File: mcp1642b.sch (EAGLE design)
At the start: 6 parts, among them U11 MCP1642B

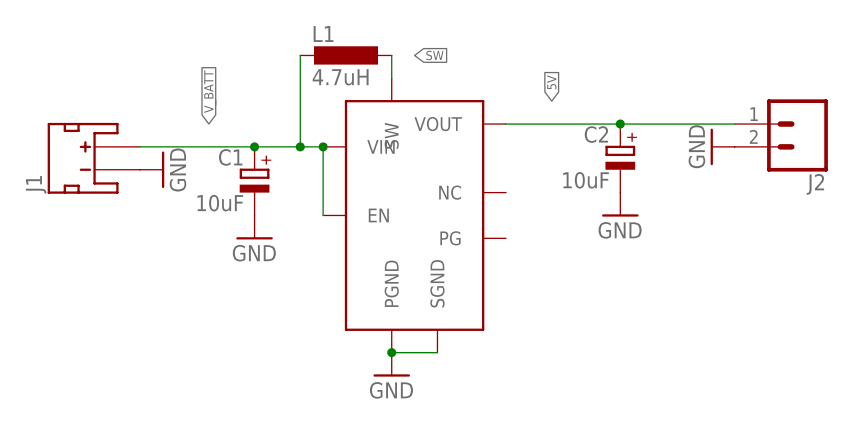
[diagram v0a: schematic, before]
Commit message: Wed  6 Mar 2019 10:52:50 EST - added AAA alkaline version of TPS61032
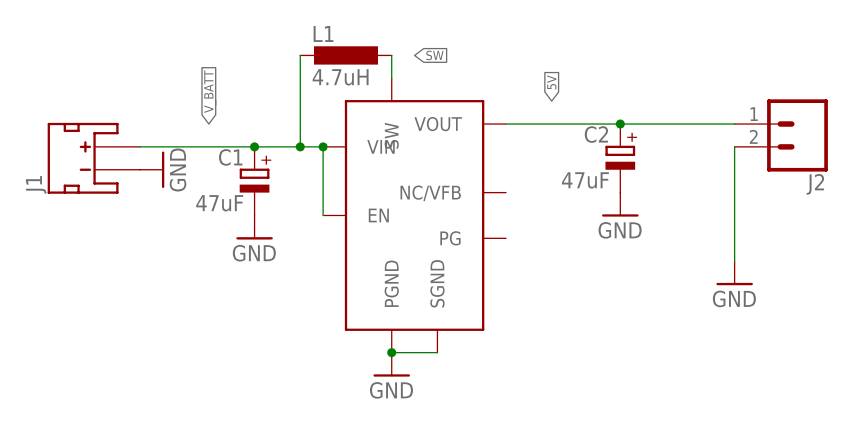
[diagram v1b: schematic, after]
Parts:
- C1, C2: value 10uF -> 47uF
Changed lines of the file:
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@@
 <?xml version="1.0" encoding="utf-8"?>
 <!DOCTYPE eagle SYSTEM "eagle.dtd">
-<eagle version="9.0.1">
+<eagle version="9.0.0">
 <drawing>
 <settings>
@@
 <grid distance="0.1" unitdist="inch" unit="inch" style="lines" multiple="1" display="no" altdistance="0.01" altunitdist="inch" altunit="inch"/>
 <layers>
-<layer number="1" name="Top" color="4" fill="1" visible="yes" active="no"/>
-<layer number="2" name="Route2" color="1" fill="3" visible="yes" active="no"/>
-<layer number="15" name="Route15" color="4" fill="6" visible="yes" active="no"/>
-<layer number="16" name="Bottom" color="1" fill="1" visible="yes" active="no"/>
-<layer number="17" name="Pads" color="2" fill="1" visible="yes" active="no"/>
-<layer number="18" name="Vias" color="2" fill="1" visible="yes" active="no"/>
-<layer number="19" name="Unrouted" color="6" fill="1" visible="yes" active="no"/>
-<layer number="20" name="Dimension" color="24" fill="1" visible="yes" active="no"/>
-<layer number="21" name="tPlace" color="7" fill="1" visible="yes" active="no"/>
-<layer number="22" name="bPlace" color="7" fill="1" visible="yes" active="no"/>
-<layer number="23" name="tOrigins" color="15" fill="1" visible="yes" active="no"/>
-<layer number="24" name="bOrigins" color="15" fill="1" visible="yes" active="no"/>
-<layer number="25" name="tNames" color="7" fill="1" visible="yes" active="no"/>
-<layer number="26" name="bNames" color="7" fill="1" visible="yes" active="no"/>
-<layer number="27" name="tValues" color="7" fill="1" visible="yes" active="no"/>
-<layer number="28" name="bValues" color="7" fill="1" visible="yes" active="no"/>
+<layer number="1" name="Top" color="4" fill="1" visible="no" active="no"/>
+<layer number="2" name="Route2" color="1" fill="3" visible="no" active="no"/>
+<layer number="15" name="Route15" color="4" fill="6" visible="no" active="no"/>
+<layer number="16" name="Bottom" color="1" fill="1" visible="no" active="no"/>
+<layer number="17" name="Pads" color="2" fill="1" visible="no" active="no"/>
+<layer number="18" name="Vias" color="2" fill="1" visible="no" active="no"/>
+<layer number="19" name="Unrouted" color="6" fill="1" visible="no" active="no"/>
+<layer number="20" name="Dimension" color="24" fill="1" visible="no" active="no"/>
+<layer number="21" name="tPlace" color="7" fill="1" visible="no" active="no"/>
+<layer number="22" name="bPlace" color="7" fill="1" visible="no" active="no"/>
+<layer number="23" name="tOrigins" color="15" fill="1" visible="no" active="no"/>
+<layer number="24" name="bOrigins" color="15" fill="1" visible="no" active="no"/>
+<layer number="25" name="tNames" color="7" fill="1" visible="no" active="no"/>
+<layer number="26" name="bNames" color="7" fill="1" visible="no" active="no"/>
+<layer number="27" name="tValues" color="7" fill="1" visible="no" active="no"/>
+<layer number="28" name="bValues" color="7" fill="1" visible="no" active="no"/>
 <layer number="29" name="tStop" color="7" fill="3" visible="no" active="no"/>
 <layer number="30" name="bStop" color="7" fill="6" visible="no" active="no"/>
@@
 <layer number="35" name="tGlue" color="7" fill="4" visible="no" active="no"/>
 <layer number="36" name="bGlue" color="7" fill="5" visible="no" active="no"/>
-<layer number="37" name="tTest" color="7" fill="1" visible="yes" active="no"/>
-<layer number="38" name="bTest" color="7" fill="1" visible="yes" active="no"/>
+<layer number="37" name="tTest" color="7" fill="1" visible="no" active="no"/>
+<layer number="38" name="bTest" color="7" fill="1" visible="no" active="no"/>
 <layer number="39" name="tKeepout" color="4" fill="11" visible="no" active="no"/>
 <layer number="40" name="bKeepout" color="1" fill="11" visible="no" active="no"/>
@@
 <layer number="44" name="Drills" color="7" fill="1" visible="no" active="no"/>
 <layer number="45" name="Holes" color="7" fill="1" visible="no" active="no"/>
-<layer number="46" name="Milling" color="3" fill="1" visible="yes" active="no"/>
-<layer number="47" name="Measures" color="7" fill="1" visible="yes" active="no"/>
-<layer number="48" name="Document" color="7" fill="1" visible="yes" active="no"/>
-<layer number="49" name="Reference" color="7" fill="1" visible="yes" active="no"/>
-<layer number="50" name="dxf" color="7" fill="1" visible="yes" active="no"/>
-<layer number="51" name="tDocu" color="7" fill="1" visible="yes" active="no"/>
-<layer number="52" name="bDocu" color="7" fill="1" visible="yes" active="no"/>
-<layer number="53" name="tGND_GNDA" color="7" fill="9" visible="yes" active="no"/>
-<layer number="54" name="bGND_GNDA" color="1" fill="9" visible="yes" active="no"/>
-<layer number="56" name="wert" color="7" fill="1" visible="yes" active="no"/>
-<layer number="57" name="tCAD" color="7" fill="1" visible="yes" active="no"/>
-<layer number="59" name="tCarbon" color="7" fill="1" visible="yes" active="no"/>
-<layer number="60" name="bCarbon" color="7" fill="1" visible="yes" active="no"/>
+<layer number="46" name="Milling" color="3" fill="1" visible="no" active="no"/>
+<layer number="47" name="Measures" color="7" fill="1" visible="no" active="no"/>
+<layer number="48" name="Document" color="7" fill="1" visible="no" active="no"/>
+<layer number="49" name="Reference" color="7" fill="1" visible="no" active="no"/>
+<layer number="50" name="dxf" color="7" fill="1" visible="no" active="no"/>
+<layer number="51" name="tDocu" color="7" fill="1" visible="no" active="no"/>
+<layer number="52" name="bDocu" color="7" fill="1" visible="no" active="no"/>
+<layer number="53" name="tGND_GNDA" color="7" fill="9" visible="no" active="no"/>
+<layer number="54" name="bGND_GNDA" color="1" fill="9" visible="no" active="no"/>
+<layer number="56" name="wert" color="7" fill="1" visible="no" active="no"/>
+<layer number="57" name="tCAD" color="7" fill="1" visible="no" active="no"/>
+<layer number="59" name="tCarbon" color="7" fill="1" visible="no" active="no"/>
+<layer number="60" name="bCarbon" color="7" fill="1" visible="no" active="no"/>
 <layer number="88" name="SimResults" color="9" fill="1" visible="yes" active="yes"/>
 <layer number="89" name="SimProbes" color="9" fill="1" visible="yes" active="yes"/>
@@
 <parts>
 <part name="U11" library="MCP1642B" deviceset="MCP1642B" device=""/>
-<part name="GND1" library="SparkFun-Aesthetics" deviceset="GND" device=""/>
+<part name="GND1" library="SparkFun-Aesthetics" library_urn="urn:adsk.eagle:library:507" deviceset="GND" device=""/>
 <part name="J1" library="SparkFun-Connectors" library_urn="urn:adsk.eagle:library:513" deviceset="JST_2MM_MALE" device="" package3d_urn="urn:adsk.eagle:package:38042/1"/>
-<part name="L1" library="rcl" deviceset="L-EU" device="WE-TPC" value="4.7uH"/>
-<part name="C1" library="rcl" deviceset="CPOL-EU" device="153CLV-0505" value="10uF"/>
-<part name="GND2" library="SparkFun-Aesthetics" deviceset="GND" device=""/>
-<part name="GND3" library="SparkFun-Aesthetics" deviceset="GND" device=""/>
-<part name="C2" library="rcl" deviceset="CPOL-EU" device="153CLV-0505" value="10uF"/>
-<part name="GND4" library="SparkFun-Aesthetics" deviceset="GND" device=""/>
+<part name="L1" library="rcl" library_urn="urn:adsk.eagle:library:334" deviceset="L-EU" device="WE-TPC" package3d_urn="urn:adsk.eagle:package:23507/1" value="4.7uH"/>
+<part name="C1" library="rcl" library_urn="urn:adsk.eagle:library:334" deviceset="CPOL-EU" device="153CLV-0505" package3d_urn="urn:adsk.eagle:package:23402/1" value="47uF"/>
+<part name="GND2" library="SparkFun-Aesthetics" library_urn="urn:adsk.eagle:library:507" deviceset="GND" device=""/>
+<part name="GND3" library="SparkFun-Aesthetics" library_urn="urn:adsk.eagle:library:507" deviceset="GND" device=""/>
+<part name="C2" library="rcl" library_urn="urn:adsk.eagle:library:334" deviceset="CPOL-EU" device="153CLV-0505" package3d_urn="urn:adsk.eagle:package:23402/1" value="47uF"/>
+<part name="GND4" library="SparkFun-Aesthetics" library_urn="urn:adsk.eagle:library:507" deviceset="GND" device=""/>
 <part name="J2" library="SparkFun-Connectors" library_urn="urn:adsk.eagle:library:513" deviceset="CONN_02" device="PTH4" package3d_urn="urn:adsk.eagle:package:38054/1"/>
-<part name="GND5" library="SparkFun-Aesthetics" deviceset="GND" device=""/>
+<part name="GND5" library="SparkFun-Aesthetics" library_urn="urn:adsk.eagle:library:507" deviceset="GND" device=""/>
 </parts>
 <sheets>
@@
 <instance part="GND4" gate="1" x="63.5" y="17.78"/>
 <instance part="J2" gate="G$1" x="83.82" y="27.94" rot="R180"/>
-<instance part="GND5" gate="1" x="73.66" y="25.4" rot="R270"/>
+<instance part="GND5" gate="1" x="76.2" y="10.16"/>
 </instances>
 <busses>
@@
 <pinref part="J2" gate="G$1" pin="2"/>
 <pinref part="GND5" gate="1" pin="GND"/>
+<wire x1="76.2" y1="12.7" x2="76.2" y2="25.4" width="0.1524" layer="91"/>
 </segment>
 </net>
@@
 packages will not be understood (or retained) with this version.
 </note>
+<note version="8.4" severity="warning">
+Since Version 8.4, EAGLE supports properties for SPICE simulation.
+Probes in schematics and SPICE mapping objects found in parts and library devices
+will not be understood with this version. Update EAGLE to the latest version
+for full support of SPICE simulation.
+</note>
 </compatibility>
